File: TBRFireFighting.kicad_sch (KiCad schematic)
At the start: 21 parts, among them J1 USB_C_Receptacle, Q1 BC817, Q2 BC817, U1 CH340G, U2 ESP32-WROOM-32UE, U3 AMS1117-3.3, Y1 12 Mhz

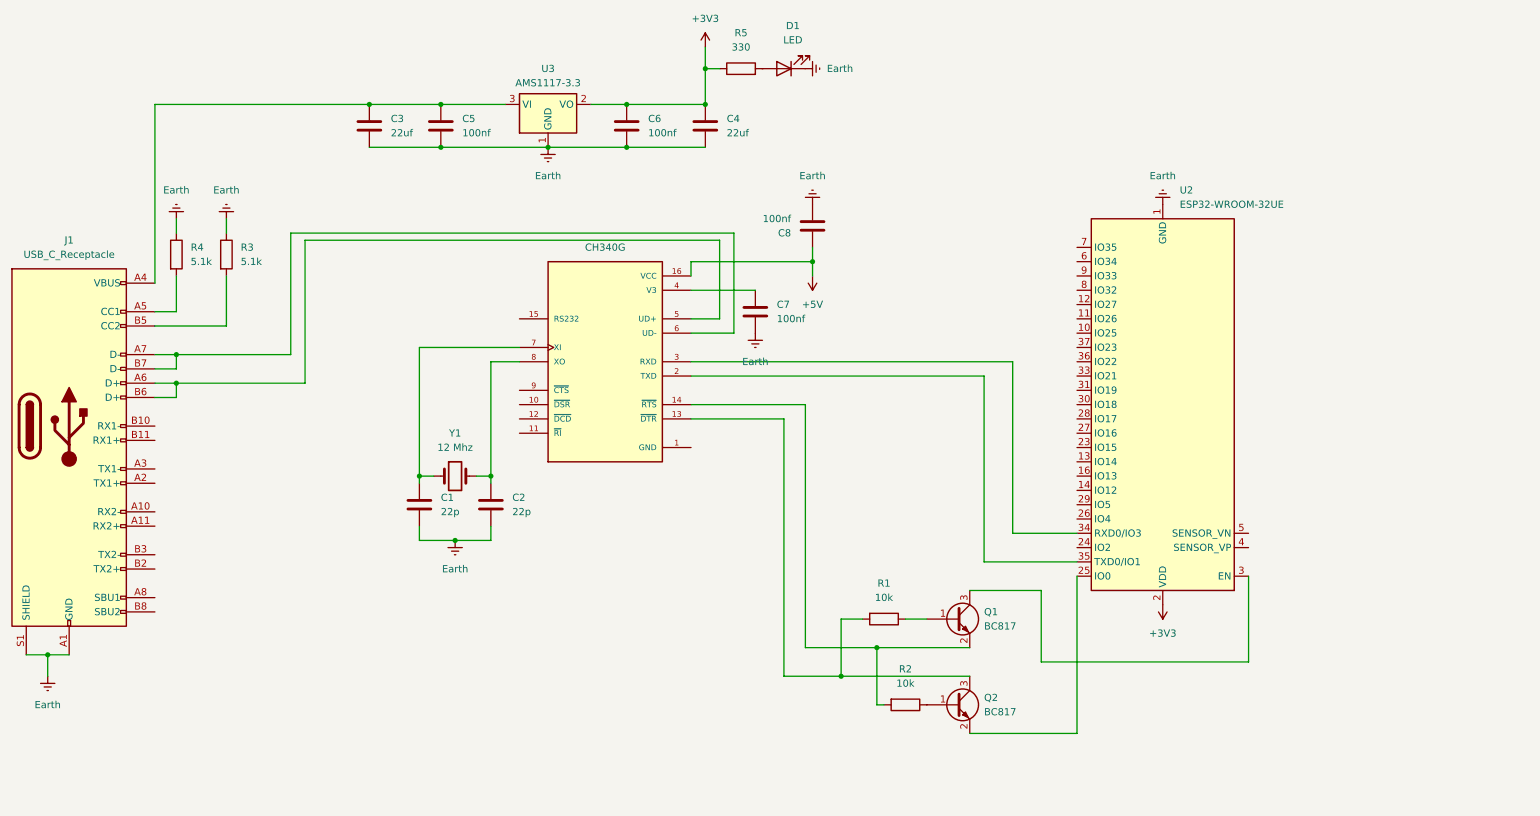
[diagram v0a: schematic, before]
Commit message: Import the TP4056
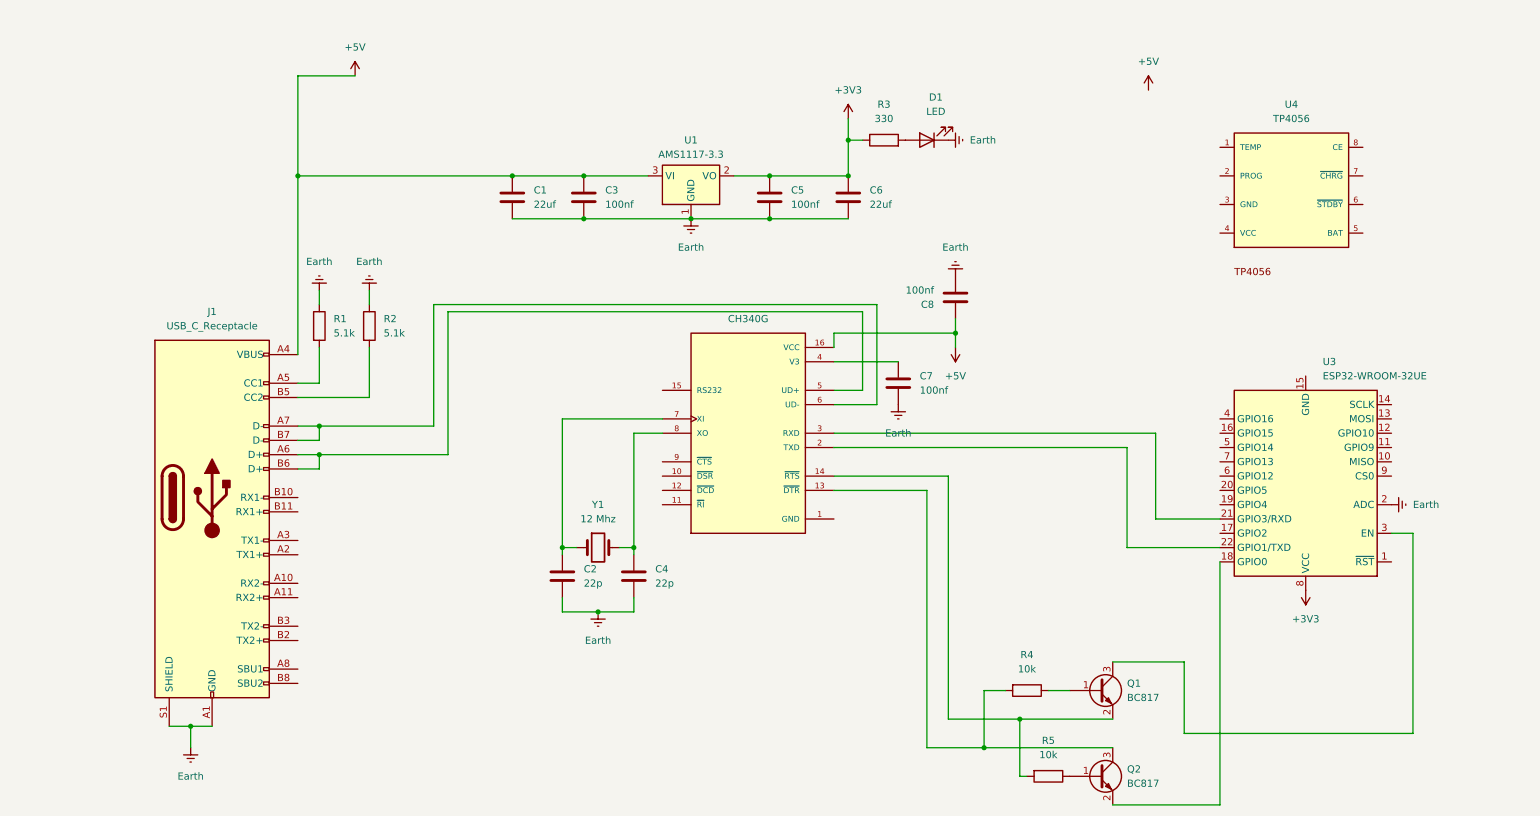
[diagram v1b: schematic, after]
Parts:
- removed U1: CH340G, CH340G:SOIC127P600X180-16N, symbol CH340G:CH340G
- removed U2: ESP32-WROOM-32UE, RF_Module:ESP32-WROOM-32UE, symbol RF_Module:ESP32-WROOM-32UE
- removed U3: AMS1117-3.3, Package_TO_SOT_SMD:SOT-223-3_TabPin2, symbol Regulator_Linear:AMS1117-3.3
- added U1: AMS1117-3.3, Package_TO_SOT_SMD:SOT-223-3_TabPin2, symbol Regulator_Linear:AMS1117-3.3
- added U2: CH340G, CH340G:SOIC127P600X180-16N, symbol CH340G:CH340G
- added U3: ESP32-WROOM-32UE, RF_Module:ESP-12E, symbol RF_Module:ESP-12F
- added U4: TP4056, TP4056:SOT23-8, symbol TP4056:TP4056
- C1: value 22p -> 22uf; footprint Capacitor_SMD:C_1206_3216Metric -> Capacitor_SMD:C_0201_0603Metric
- C3: value 22uf -> 100nf
- C4: value 22uf -> 22p; footprint Capacitor_SMD:C_0201_0603Metric -> Capacitor_SMD:C_1206_3216Metric
- C6: value 100nf -> 22uf
- R1, R2: value 10k -> 5.1k
- R3: value 5.1k -> 330; footprint Resistor_SMD:R_1206_3216Metric -> Resistor_SMD:R_0201_0603Metric
- R4: value 5.1k -> 10k
- R5: value 330 -> 10k; footprint Resistor_SMD:R_0201_0603Metric -> Resistor_SMD:R_1206_3216Metric
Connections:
- net +3V3: now also C5.1, R3.1, U1.2 (VO), U3.8 (VCC); no longer C4.1, R5.1
- net +5V: now also C1.1, C3.1, J1.A4 (VBUS), J1.A9 (VBUS), J1.B4 (VBUS), J1.B9 (VBUS), U1.3 (VI), U2.16 (VCC)
- net Earth: now also R1.1, R2.1, U1.1 (GND), U3.2 (ADC); no longer R3.1, R4.1
- net at Q2.1 (B): now also R5.1; no longer R2.1
- net at R2.2: now also J1.B5 (CC2); no longer Q1.2 (E)
- net at Q2.2 (E): now also U3.18 (GPIO0)
- net at R1.2: now also J1.A5 (CC1); no longer Q2.3 (C)
- net at R5.2: now also Q1.2 (E), U2.14 (~{RTS}); no longer D1.2 (A)
- net at Q1.1 (B): now also R4.1; no longer R1.1
- net at Q1.3 (C): now also U3.3 (EN)
- net at Y1.2: now also C4.1, U2.8 (XO); no longer C2.1
- net at R4.2: now also Q2.3 (C), U2.13 (~{DTR}); no longer J1.A5 (CC1)
- net at J1.A6 (D+), J1.B6 (D+): now also U2.5 (UD+)
- net at J1.A7 (D-), J1.B7 (D-): now also U2.6 (UD-)
- net at R3.2: now also D1.2 (A); no longer J1.B5 (CC2)
- net at C7.1: now also U2.4 (V3)
- net at Y1.1: now also C2.1, U2.7 (XI); no longer C1.1
- new net: U2.3 (RXD), U3.21 (GPIO3/RXD)
- new net: U2.2 (TXD), U3.22 (GPIO1/TXD)

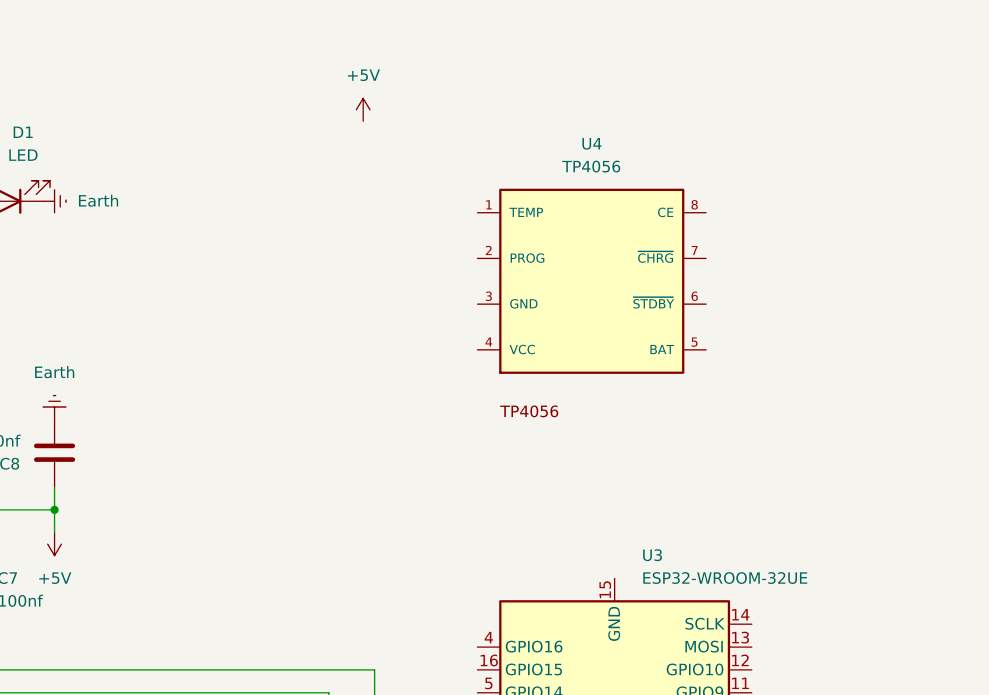
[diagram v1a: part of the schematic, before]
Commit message: updated schematic with TP4056
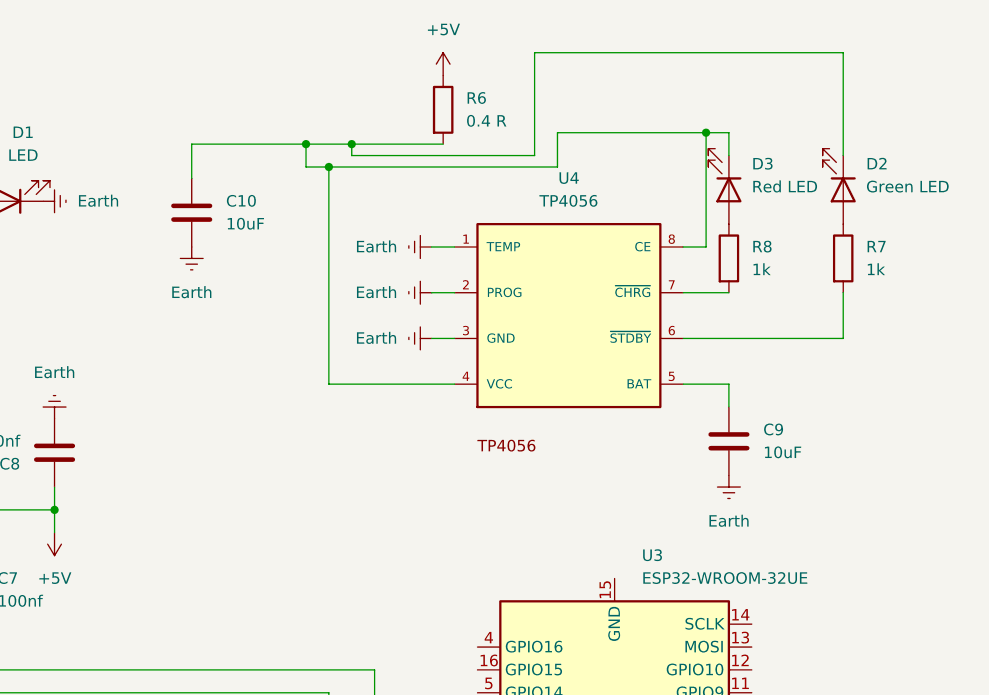
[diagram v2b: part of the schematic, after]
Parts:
- added C10, C9: 10uF, symbol Device:C
- added D2: Green LED, symbol Device:LED
- added D3: Red LED, symbol Device:LED
- added R6: 0.4 R, Resistor_SMD:R_1206_3216Metric, symbol Device:R
- added R7, R8: 1k, Resistor_SMD:R_1206_3216Metric, symbol Device:R
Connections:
- net +5V: now also R6.1
- net Earth: now also U4.1 (TEMP), U4.2 (PROG), U4.3 (GND), C10.2, C9.2
- net at U4.4 (VCC): now also U4.8 (CE), C10.1, D2.1 (K), D3.1 (K), R6.2
- net at U4.5 (BAT): now also C9.1
- net at U4.6 (~{STDBY}): now also R7.2
- net at U4.7 (~{CHRG}): now also R8.2
- new net: D3.2 (A), R8.1
- new net: D2.2 (A), R7.1
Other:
- moved on the sheet: U4
